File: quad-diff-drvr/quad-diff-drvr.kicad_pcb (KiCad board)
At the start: 2 copper layers, 65 x 56 mm, 10 parts, among them J1 Raspberry_Pi_2_3, J2 Conn_01x04, J3 Conn_01x04, J4 Conn_01x04, J5 Conn_01x04, J6 Conn_01x04

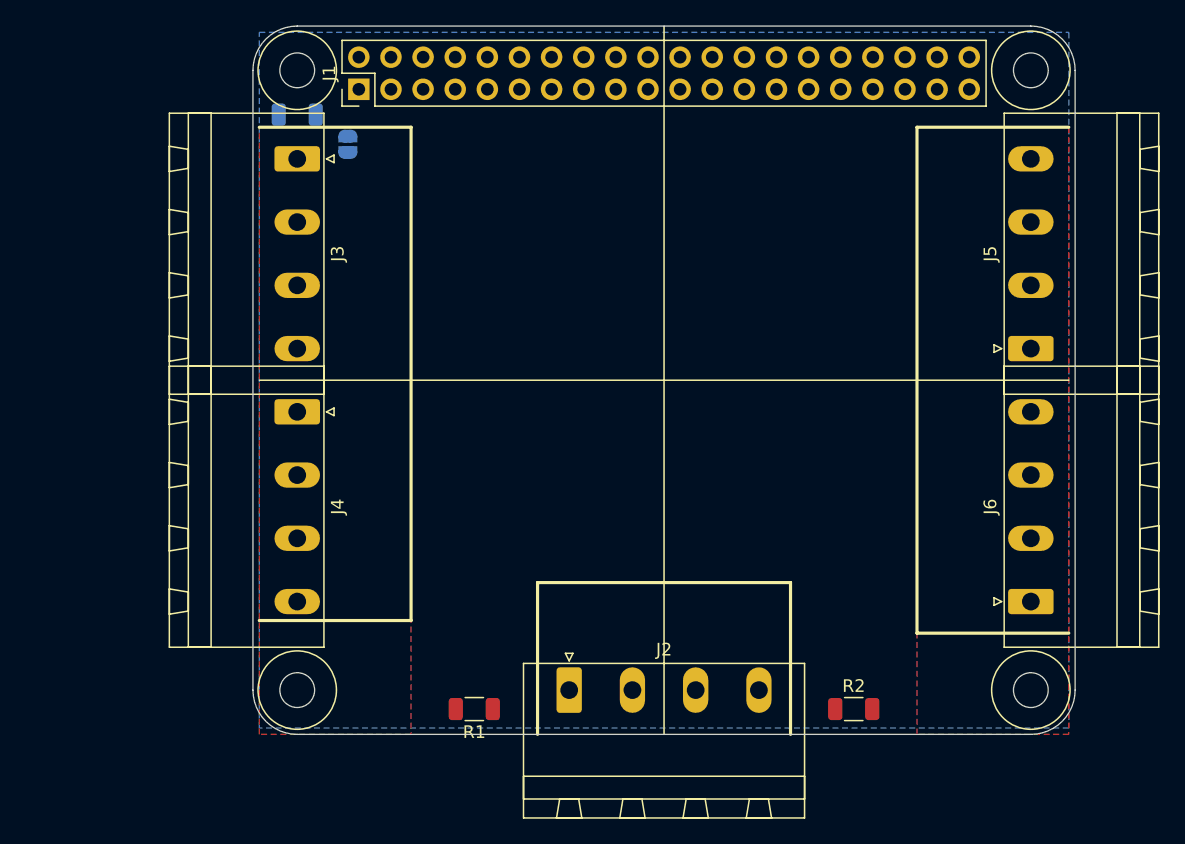
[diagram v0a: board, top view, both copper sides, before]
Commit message: qdd: power monitor added
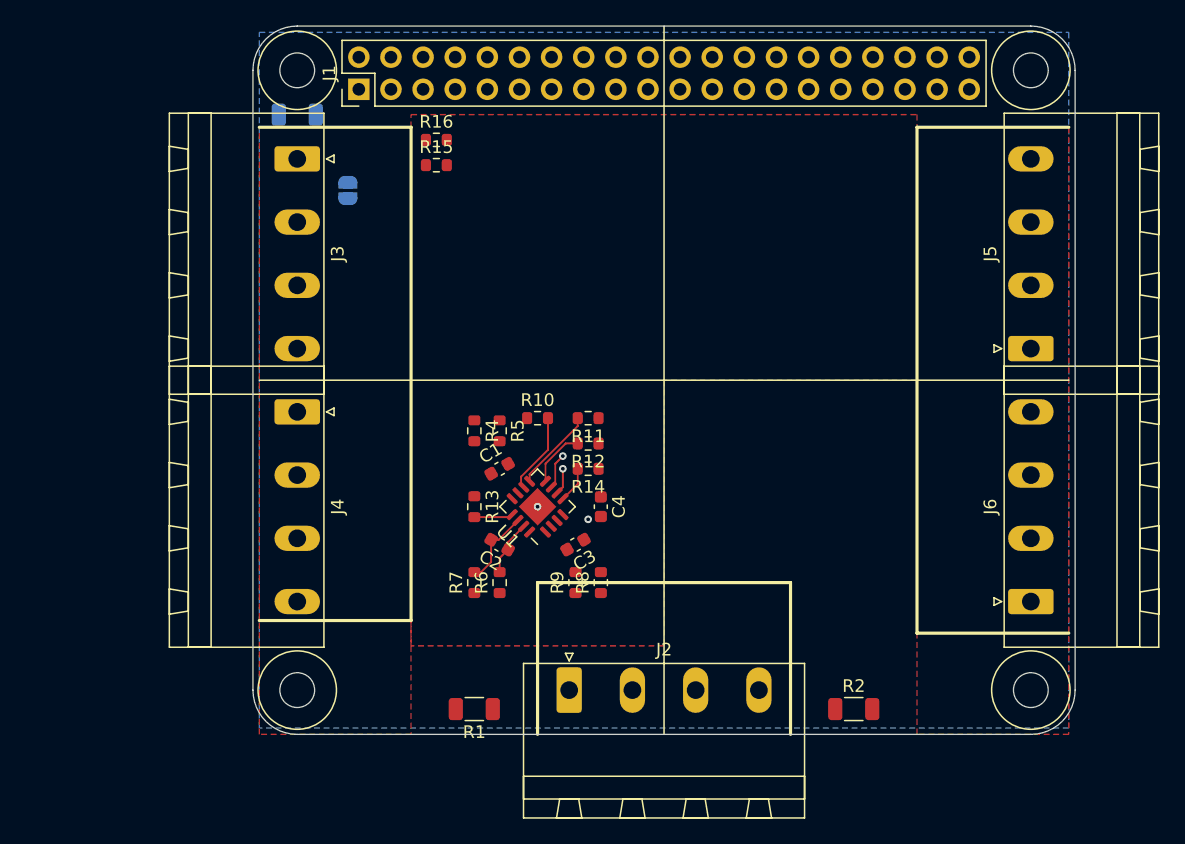
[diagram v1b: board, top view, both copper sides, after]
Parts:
- added C1: 100nF, Capacitor_SMD:C_0603_1608Metric, F.Cu at (87.0, 107.0)
- added C2: 100nF, Capacitor_SMD:C_0603_1608Metric, F.Cu at (87.0, 113.0)
- added C3: 100nF, Capacitor_SMD:C_0603_1608Metric, F.Cu at (93.0, 113.0)
- added C4: 100nF, Capacitor_SMD:C_0603_1608Metric, F.Cu at (95.0, 110.0)
- added R10: 10k, Resistor_SMD:R_0603_1608Metric, F.Cu at (90.0, 103.0)
- added R11: 10k, Resistor_SMD:R_0603_1608Metric, F.Cu at (94.0, 103.0)
- added R12: 10k, Resistor_SMD:R_0603_1608Metric, F.Cu at (94.0, 105.0)
- added R13: 10k, Resistor_SMD:R_0603_1608Metric, F.Cu at (85.0, 110.0)
- added R14: 10k, Resistor_SMD:R_0603_1608Metric, F.Cu at (94.0, 107.0)
- added R15: R, Resistor_SMD:R_0603_1608Metric, F.Cu at (82.0, 83.0)
- added R16: R, Resistor_SMD:R_0603_1608Metric, F.Cu at (82.0, 81.0)
- added R4: 10R, Resistor_SMD:R_0603_1608Metric, F.Cu at (85.0, 104.0)
- added R5: 10R, Resistor_SMD:R_0603_1608Metric, F.Cu at (87.0, 104.0)
- added R6: 10R, Resistor_SMD:R_0603_1608Metric, F.Cu at (87.0, 116.0)
- added R7: 10R, Resistor_SMD:R_0603_1608Metric, F.Cu at (85.0, 116.0)
- added R8: 10R, Resistor_SMD:R_0603_1608Metric, F.Cu at (95.0, 116.0)
- added R9: 10R, Resistor_SMD:R_0603_1608Metric, F.Cu at (93.0, 116.0)
- added U1: INA3221, Package_DFN_QFN:Texas_RGV_S-PVQFN-N16_EP2.1x2.1mm, F.Cu at (90.0, 110.0)
- moved JP1 3.65 mm to (75.0, 85.0)
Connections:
- net Net-(JP1-Pad1) renamed /5V_SENSE
- J1 pad 1: (no net) -> +3V3
- J1 pad 17: (no net) -> +3V3
- J1 pad 3: (no net) -> /SDA
- J1 pad 5: (no net) -> /SCL
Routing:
- net /PM_CRIT: track 0.00 -> 6.57 mm
- net /PM_PV: track 0.00 -> 6.42 mm
- net Net-(C2-Pad2): track 0.00 -> 6.18 mm
- net /PM_WARN: track 0.00 -> 4.61 mm
- net Net-(C2-Pad1): track 0.00 -> 4.42 mm
- net /PM_TC: track 0.00 -> 3.08 mm
- net /PM_A0: track 0.00 -> 2.86 mm
- net /SDA: track 0.00 -> 2.83 mm, vias 0 -> 1
- net /SCL: track 0.00 -> 2.10 mm, vias 0 -> 1
- net GND: vias 0 -> 2
- added copper zone on F.Cu, net +3V3

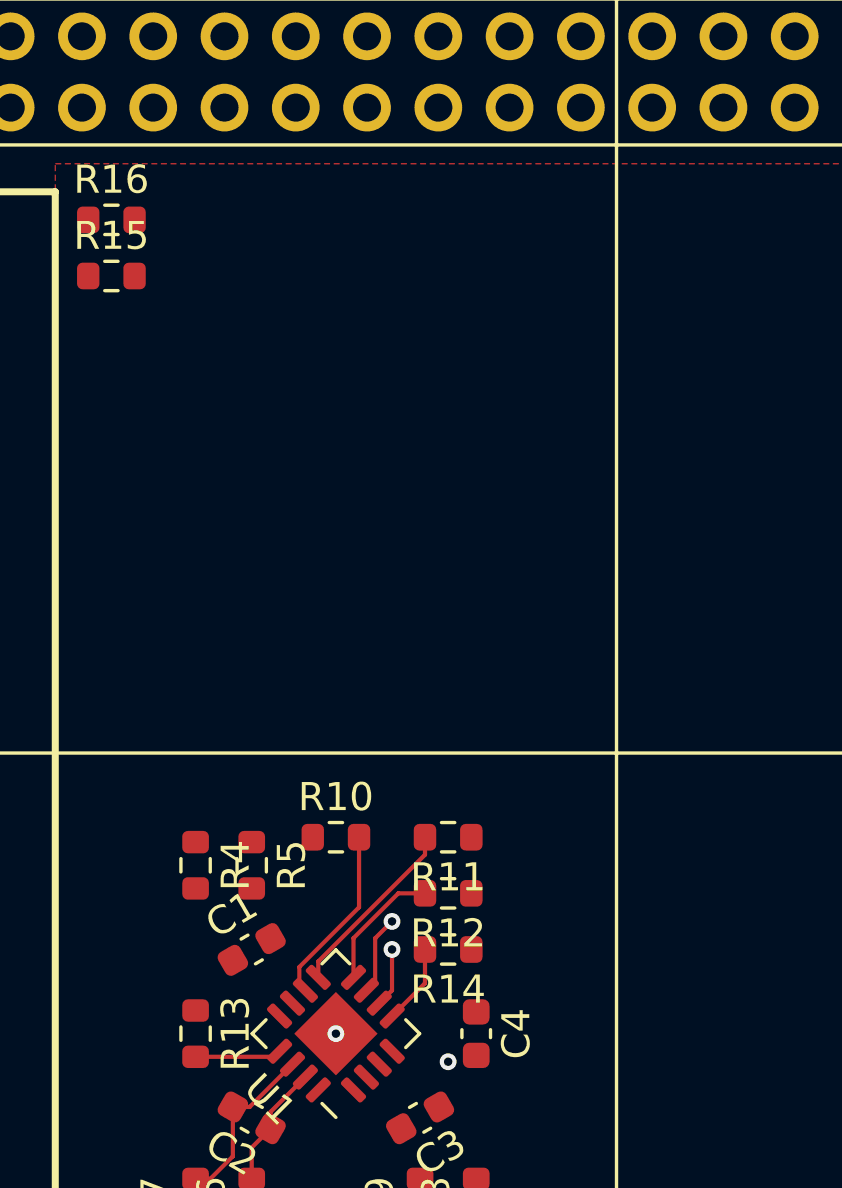
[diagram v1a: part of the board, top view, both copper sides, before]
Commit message: qdd: add mux0 and mux1
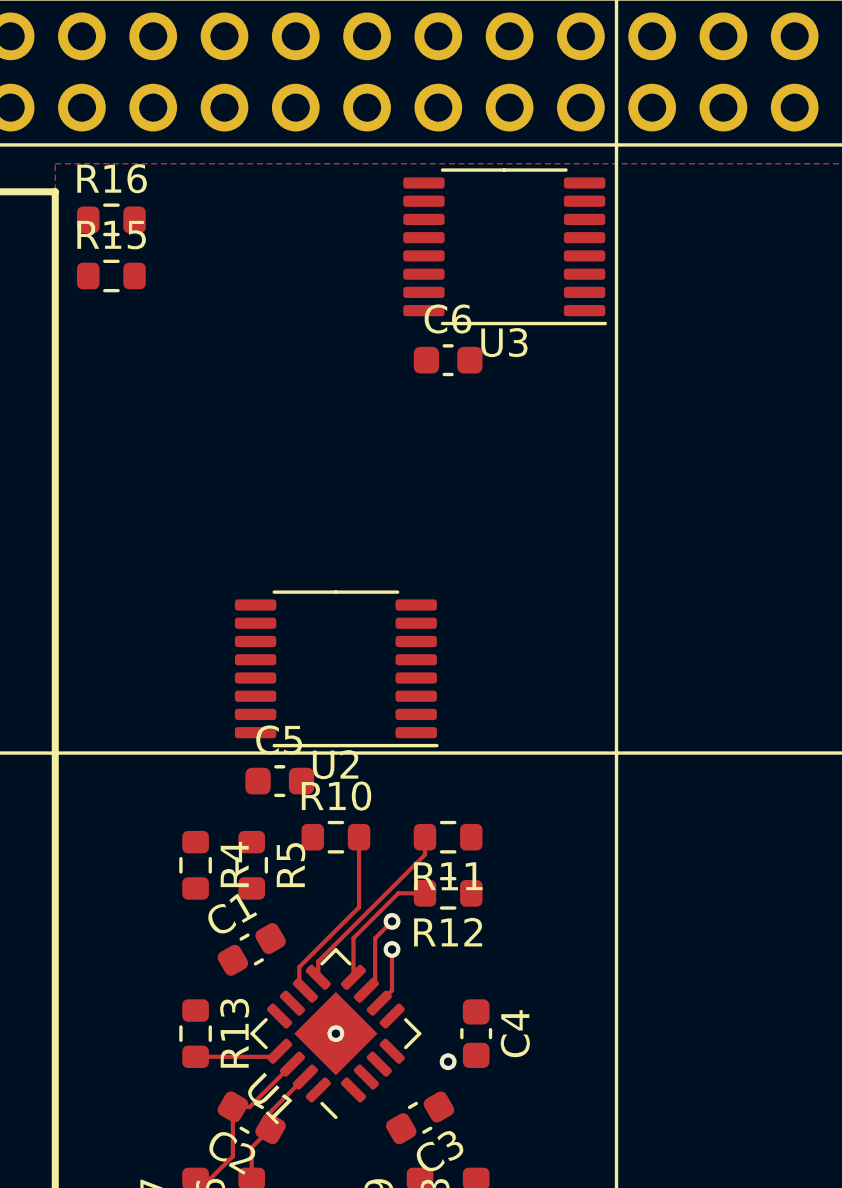
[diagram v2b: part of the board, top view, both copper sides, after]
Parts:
- removed R14: 10k, Resistor_SMD:R_0603_1608Metric
- added C5: 100nF, Capacitor_SMD:C_0603_1608Metric, F.Cu at (88.0, 101.0)
- added C6: 100nF, Capacitor_SMD:C_0603_1608Metric, F.Cu at (94.0, 86.0)
- added U2: 74LS153, Package_SO:TSSOP-16_4.4x5mm_P0.65mm, F.Cu at (90.0, 97.0)
- added U3: 74LS153, Package_SO:TSSOP-16_4.4x5mm_P0.65mm, F.Cu at (96.0, 82.0)
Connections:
- J1 pad 10: (no net) -> /SD7
- J1 pad 19: (no net) -> /SD2
- J1 pad 21: (no net) -> /SD1
- J1 pad 23: (no net) -> /SD3
- J1 pad 24: (no net) -> /SD0
- J1 pad 32: (no net) -> /SD4
- J1 pad 33: (no net) -> /SD5
- J1 pad 8: (no net) -> /SD6
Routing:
- net /PM_A0: track 2.86 -> 0.00 mm

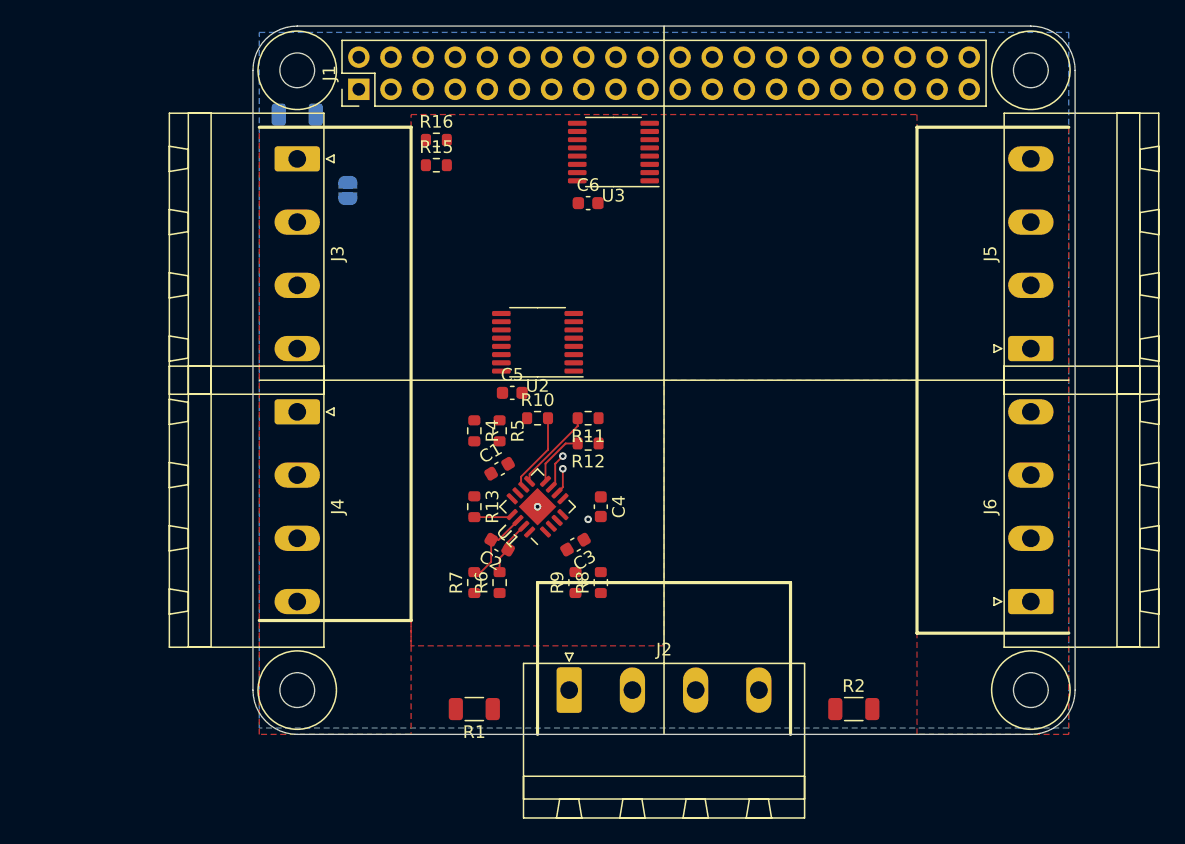
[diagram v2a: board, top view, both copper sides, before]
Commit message: qd: GPIO expander in
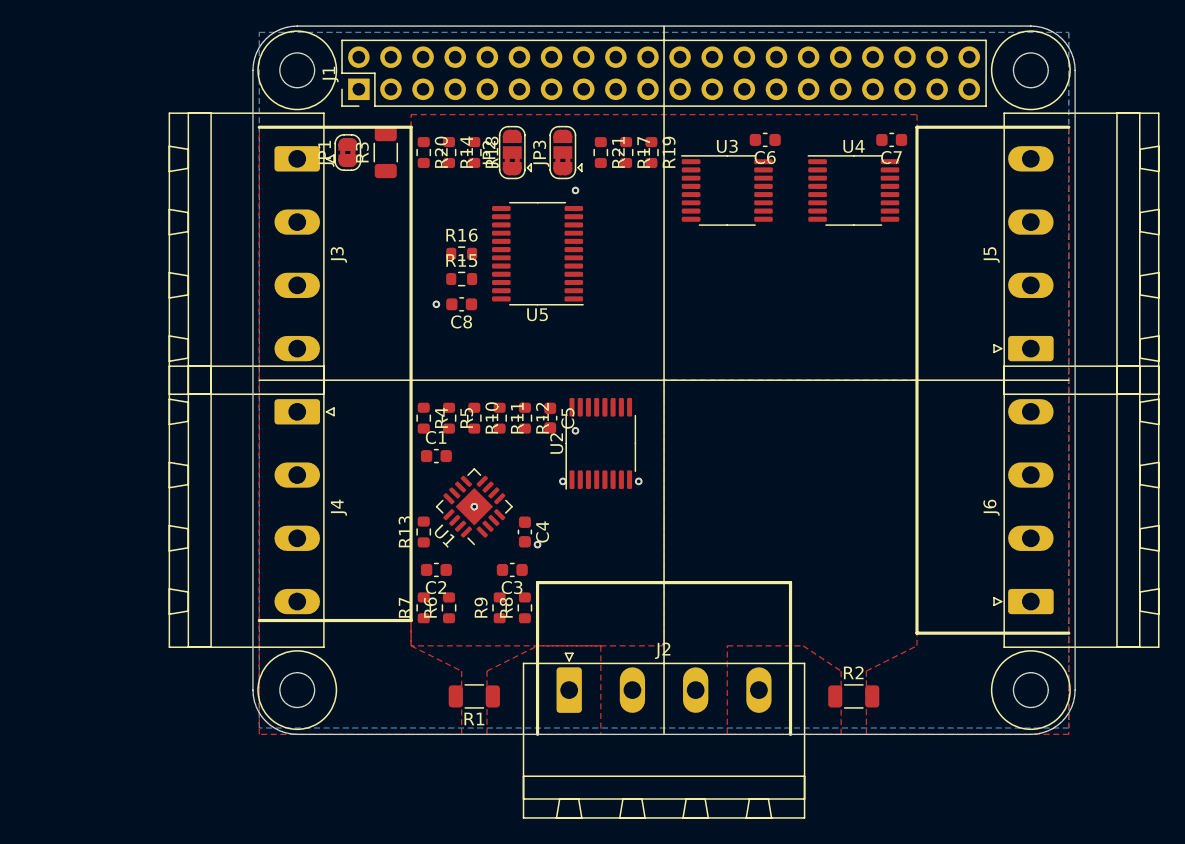
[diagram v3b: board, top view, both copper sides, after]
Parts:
- added C7: 100nF, Capacitor_SMD:C_0603_1608Metric, F.Cu at (118.0, 81.0)
- added C8: 100nF, Capacitor_SMD:C_0603_1608Metric, F.Cu at (84.0, 94.0)
- added JP2: SolderJumper_3_Bridged12, Jumper:SolderJumper-3_P1.3mm_Bridged2Bar12_RoundedPad1.0x1.5mm, F.Cu at (88.0, 82.0)
- added JP3: SolderJumper_3_Bridged12, Jumper:SolderJumper-3_P1.3mm_Bridged2Bar12_RoundedPad1.0x1.5mm, F.Cu at (92.0, 82.0)
- added R14: 10k, Resistor_SMD:R_0603_1608Metric, F.Cu at (83.0, 82.0)
- added R17: 10k, Resistor_SMD:R_0603_1608Metric, F.Cu at (97.0, 82.0)
- added R18: 10k, Resistor_SMD:R_0603_1608Metric, F.Cu at (85.0, 82.0)
- added R19: 10k, Resistor_SMD:R_0603_1608Metric, F.Cu at (99.0, 82.0)
- added R20: 10k, Resistor_SMD:R_0603_1608Metric, F.Cu at (81.0, 82.0)
- added R21: 10k, Resistor_SMD:R_0603_1608Metric, F.Cu at (95.0, 82.0)
- added U4: 74LS153, Package_SO:TSSOP-16_4.4x5mm_P0.65mm, F.Cu at (115.0, 85.0)
- added U5: PCA9555PW, Package_SO:TSSOP-24_4.4x7.8mm_P0.65mm, F.Cu at (90.0, 90.0)
- JP1: value SolderJumper_2_Open -> SolderJumper_2_Bridged; footprint Jumper:SolderJumper-2_P1.3mm_Open_RoundedPad1.0x1.5mm -> Jumper:SolderJumper-2_P1.3mm_Bridged2Bar_RoundedPad1.0x1.5mm; moved to F.Cu
- R15, R16: value R -> 10k
- R3: moved to F.Cu
- moved C6 14.9 mm to (108.0, 81.0), turned to 180 degrees
- moved U3 9.50 mm to (105.0, 85.0), turned to 0 degrees
- moved U2 9.43 mm to (95.0, 105.0), turned to 90 degrees
- moved R15 9.22 mm to (84.0, 92.0)
- moved R16 9.22 mm to (84.0, 90.0)
- moved R3 7.62 mm to (78.0, 82.0), turned to 90 degrees
- moved R11 7.00 mm to (87.0, 103.0), turned to 270 degrees
- moved C4 6.32 mm to (89.0, 112.0)
- moved R8 6.32 mm to (89.0, 118.0)
- moved R9 6.32 mm to (87.0, 118.0)
- moved C2 5.39 mm to (82.0, 115.0), turned to 180 degrees
- moved C3 5.39 mm to (88.0, 115.0), turned to 180 degrees
- moved R12 5.39 mm to (89.0, 103.0), turned to 270 degrees
- moved C1 5.10 mm to (82.0, 106.0), turned to 0 degrees
- moved R10 5.00 mm to (85.0, 103.0), turned to 270 degrees
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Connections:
- J1 pad 11: (no net) -> /SD9
- J1 pad 12: (no net) -> /SD10
- J1 pad 15: (no net) -> /SD14
- J1 pad 16: (no net) -> /SD15
- J1 pad 35: (no net) -> /SD11
- J1 pad 36: (no net) -> /SD8
- J1 pad 38: (no net) -> /SD12
- J1 pad 40: (no net) -> /SD13
- J2 pad 3: /VB_SENSE -> GND
- J2 pad 4: GND -> /VB_SENSE
- JP1 pad 1: /5V_SENSE -> /VA
- JP1 pad 2: /VA -> /5V_SENSE
- U1 pad 5: /PM_A0 -> /PM_ASEL
- U2 pad 14: /A0 -> /PM_A0
- U2 pad 2: /A1 -> /PM_A1
- U2 pad 7: /PM_A0 -> /PM_ASEL
- U2 pad 9: (no net) -> /PM_STAT
- U3 pad 10: /SD4 -> /SD14
- U3 pad 11: /SD5 -> /SD15
- U3 pad 12: /SD6 -> /SD0
- U3 pad 13: /SD7 -> /SD1
- U3 pad 14: /A0 -> /M0_A0
- U3 pad 2: /A1 -> /M0_A1
- U3 pad 3: /SD3 -> /SD10
- U3 pad 4: /SD2 -> /SD9
- U3 pad 5: /SD1 -> /SD7
- U3 pad 6: /SD0 -> /SD6
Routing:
- net /PM_CRIT: track 6.57 -> 0.00 mm
- net /PM_PV: track 6.42 -> 0.00 mm
- net Net-(C2-Pad2): track 6.18 -> 0.00 mm
- net /PM_WARN: track 4.61 -> 0.00 mm
- net Net-(C2-Pad1): track 4.42 -> 0.00 mm
- net /PM_TC: track 3.08 -> 0.00 mm
- net /SDA: track 2.83 -> 0.00 mm, vias 1 -> 0
- net /SCL: track 2.10 -> 0.00 mm, vias 1 -> 0
- net GND: vias 2 -> 7
- added copper zone on F.Cu, net /VA_SENSE
- added copper zone on F.Cu, net /VB_SENSE

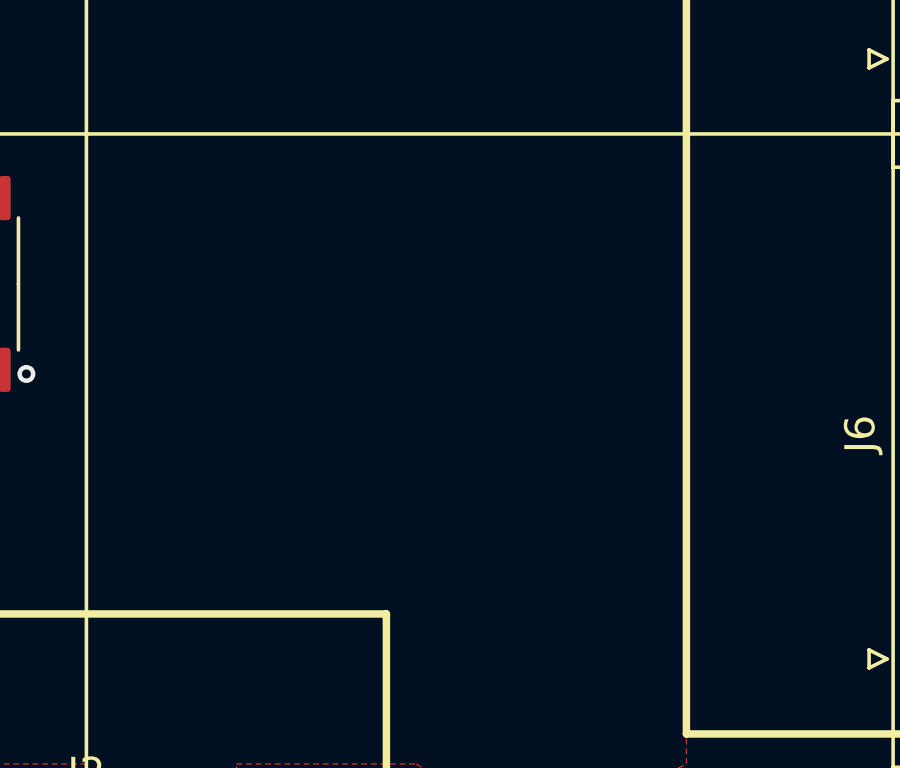
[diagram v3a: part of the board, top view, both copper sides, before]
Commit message: qdd: driver added
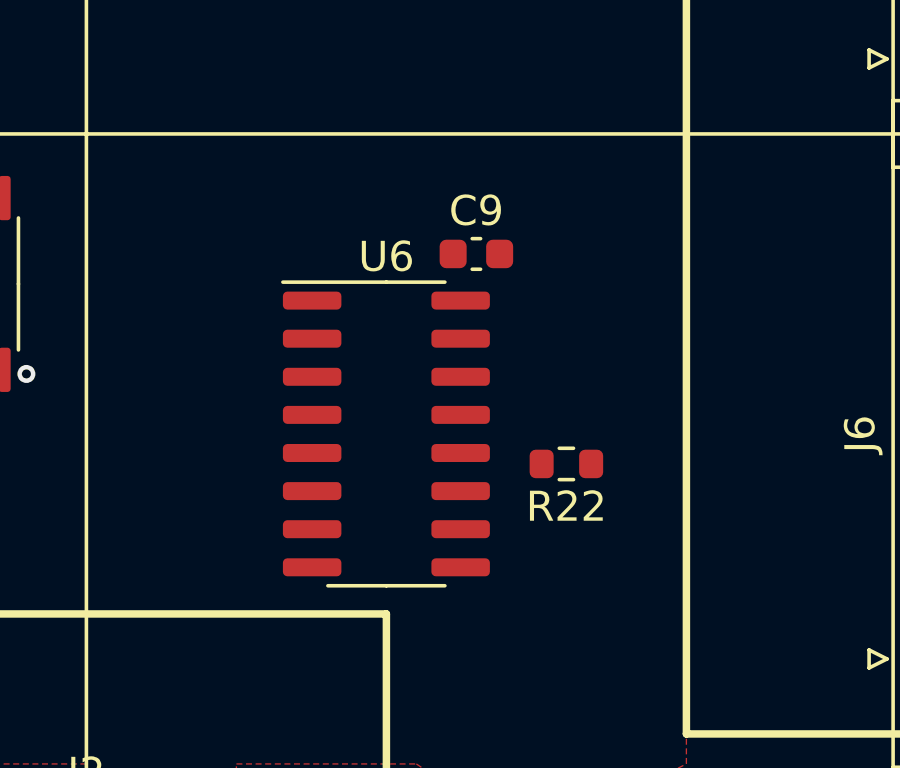
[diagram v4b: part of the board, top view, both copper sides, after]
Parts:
- added C9: 100nF, Capacitor_SMD:C_0603_1608Metric, F.Cu at (113.0, 104.0)
- added R22: 10k, Resistor_SMD:R_0603_1608Metric, F.Cu at (116.0, 111.0)
- added U6: LTC1688, Package_SO:SOIC-16_3.9x9.9mm_P1.27mm, F.Cu at (110.0, 110.0)
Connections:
- J3 pad 3: (no net) -> /D0+
- J3 pad 4: (no net) -> /D0-
- J4 pad 3: (no net) -> /D1+
- J4 pad 4: (no net) -> /D1-
- J5 pad 3: (no net) -> /D2+
- J5 pad 4: (no net) -> /D2-
- J6 pad 3: (no net) -> /D3+
- J6 pad 4: (no net) -> /D3-
- U3 pad 7: (no net) -> /D0
- U3 pad 9: (no net) -> /D1
- U4 pad 7: (no net) -> /D2
- U4 pad 9: (no net) -> /D3
- U5 pad 16: (no net) -> /DEN
